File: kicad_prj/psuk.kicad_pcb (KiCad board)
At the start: 2 copper layers, 39 parts, among them J1 ATABA S-360-12 connector, J5 XT-60F, Q1 AOD240, Q2 AOD240, U1 OPA189IDR, U2 TL431DBZ, U3 TL431DBZ, U4 LM397

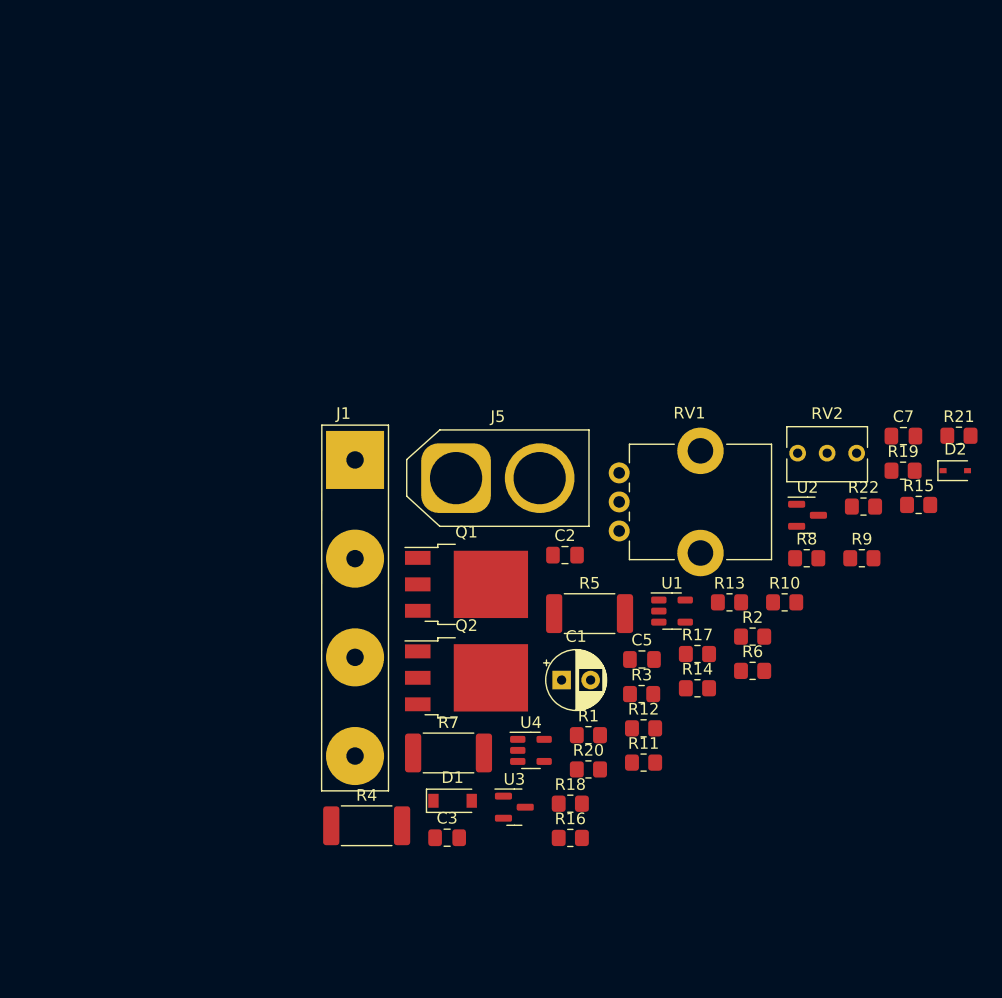
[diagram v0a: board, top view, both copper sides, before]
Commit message: Updated schematics. Fixed wrong and missing 3D models.
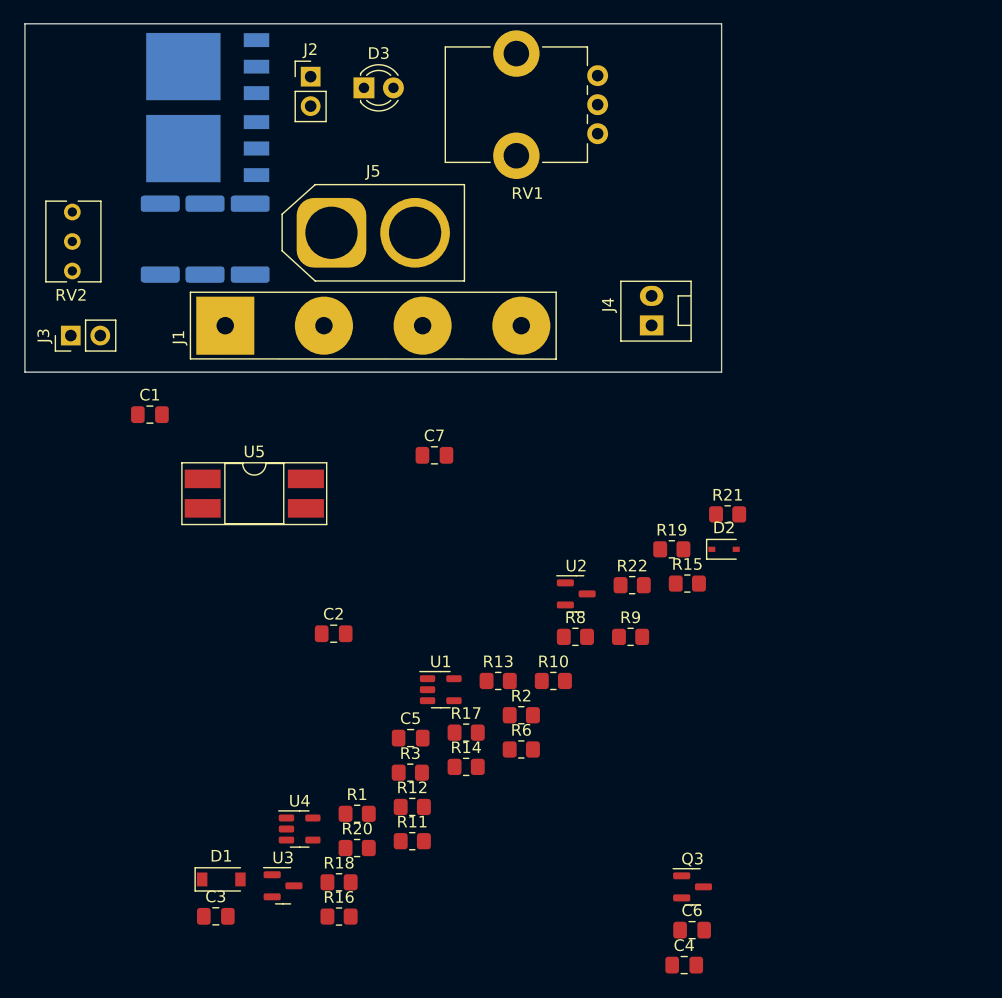
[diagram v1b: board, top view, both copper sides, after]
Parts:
- added C4: 150pF, Capacitor_SMD:C_0805_2012Metric_Pad1.18x1.45mm_HandSolder, F.Cu at (119.8, 121.1)
- added C6: 1n, Capacitor_SMD:C_0805_2012Metric_Pad1.18x1.45mm_HandSolder, F.Cu at (120.5, 118.1)
- added D3: YEL-3mm, LED_THT:LED_D3.0mm, F.Cu at (92.2, 45.5)
- added J2: 22-23-2021, Connector_PinHeader_2.54mm:PinHeader_1x02_P2.54mm_Vertical, F.Cu at (87.6, 44.6)
- added J3: 22-23-2021, Connector_PinHeader_2.54mm:PinHeader_1x02_P2.54mm_Vertical, F.Cu at (66.9, 66.9)
- added J4: XH2.54-2P, psuk:FanPinHeader_1x02_P2.54mm_Vertical, F.Cu at (117.0, 66.0)
- added Q3: IRLML2502TRPBF, Package_TO_SOT_SMD:SOT-23, F.Cu at (120.5, 114.3)
- added U5: FOD817B3SD, Package_DIP:DIP-4_W8.89mm_SMDSocket_LongPads, F.Cu at (82.8, 80.5)
- C1: value 22uF -> 10u/25V; footprint Capacitor_THT:CP_Radial_D5.0mm_P2.50mm -> Capacitor_SMD:C_0805_2012Metric_Pad1.18x1.45mm_HandSolder
- Q1, Q2, R4, R5, R7: moved to B.Cu
- moved RV2 70.7 mm to (67.1, 56.2), turned to 90 degrees
- moved R4 53.6 mm to (74.7, 58.5), turned to -90 degrees
- moved Q2 50.7 mm to (78.7, 50.7), turned to 180 degrees
- moved Q1 49.9 mm to (78.7, 43.7), turned to 180 degrees
- moved R7 47.4 mm to (82.4, 58.5), turned to -90 degrees
- moved R5 46.2 mm to (78.5, 58.5), turned to -90 degrees
- moved C1 42.2 mm to (73.8, 73.7)
- moved C7 40.4 mm to (98.3, 77.2)
- moved RV1 39.3 mm to (112.3, 44.5), turned to 180 degrees
- moved J5 23.7 mm to (89.4, 58.0)
- moved R8 21.0 mm to (110.4, 92.8)
- moved R9 21.0 mm to (115.2, 92.8)
- moved C3 21.0 mm to (79.4, 116.9)
- moved D2 21.0 mm to (123.2, 85.3)
- moved R1 21.0 mm to (91.6, 108.0)
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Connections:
- C1 pad 1: Net-(C1-Pad1) -> GND
- C1 pad 2: GND -> Net-(D1-Pad1)
- D1 pad 1: Net-(C1-Pad1) -> Net-(D1-Pad1)
- R1 pad 1: Net-(C1-Pad1) -> Net-(D1-Pad1)
- R2 pad 1: Net-(C1-Pad1) -> Net-(D1-Pad1)
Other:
- board outline added: 60 x 30 mm

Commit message: Completed PCB routing. Released v1.0 artifact for production and procurement purposes.
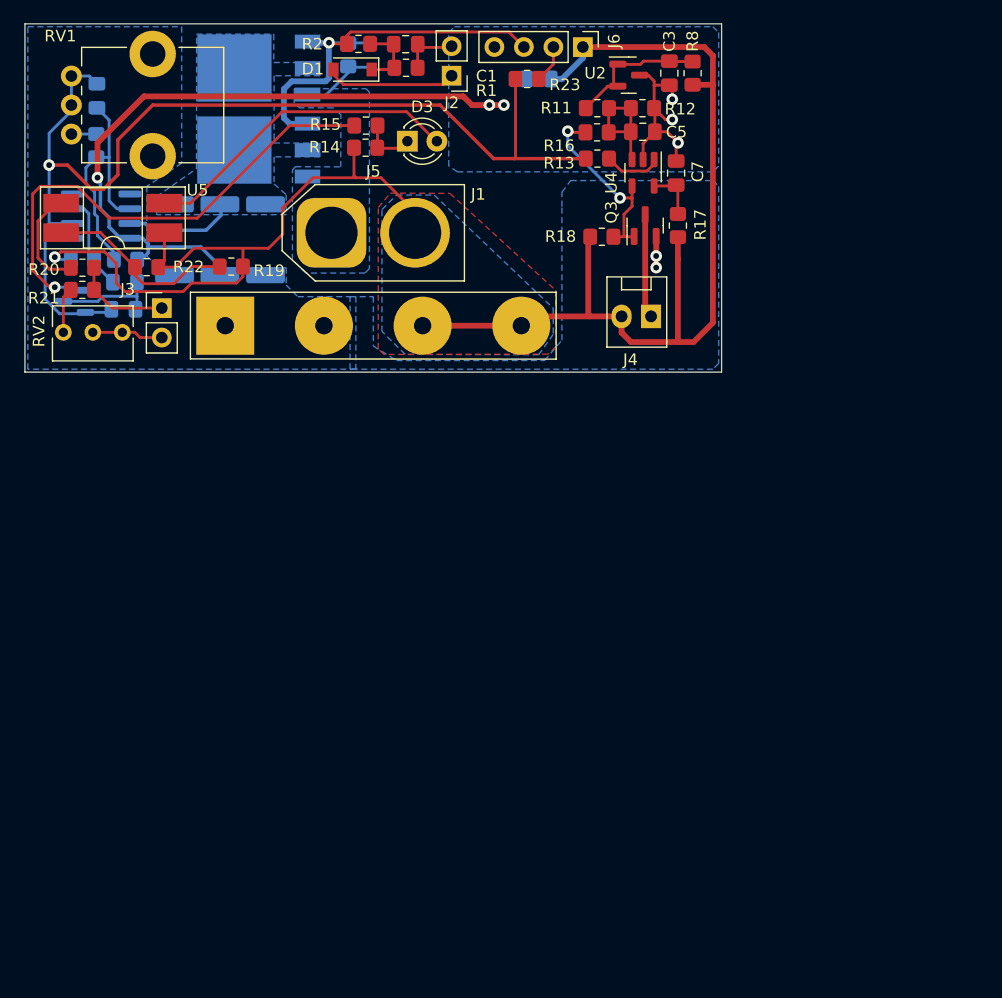
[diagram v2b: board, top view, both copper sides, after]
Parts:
- added C8: 100n, Capacitor_SMD:C_0805_2012Metric_Pad1.18x1.45mm_HandSolder, B.Cu at (107.2, 44.8)
- added J6: Conn_01x04_Male, Connector_PinHeader_2.54mm:PinHeader_1x04_P2.54mm_Vertical, F.Cu at (111.0, 42.0)
- added R23: 47, Resistor_SMD:R_0805_2012Metric_Pad1.20x1.40mm_HandSolder, F.Cu at (106.2, 44.8)
- C2, C4, C6, D2, R10, R3, R6, R9, U3: moved to B.Cu
- R16: value 220k -> 1M
- U1: footprint Package_TO_SOT_SMD:TSOT-23-5 -> Package_SO:SOIC-8_3.9x4.9mm_P1.27mm; moved to B.Cu
- moved C4 90.4 mm to (69.2, 46.2), turned to -90 degrees
- moved C3 82.5 mm to (118.5, 44.2), turned to 90 degrees
- moved C6 72.5 mm to (71.5, 64.6), turned to 180 degrees
- moved R16 71.1 mm to (112.3, 49.3), turned to 180 degrees
- moved D1 70.7 mm to (91.2, 43.9), turned to 180 degrees
- moved R11 65.1 mm to (112.3, 47.3)
- moved R1 64.4 mm to (95.8, 43.8)
- moved U4 63.8 mm to (116.2, 52.8), turned to -90 degrees
- moved R12 63.4 mm to (116.2, 47.3)
- moved R9 62.5 mm to (69.1, 50.5), turned to 90 degrees
- moved R3 62.1 mm to (90.8, 42.7), turned to -90 degrees
- moved R18 60.0 mm to (112.7, 58.3), turned to 180 degrees
- moved R2 59.5 mm to (91.7, 41.7), turned to 180 degrees
- moved R21 58.8 mm to (67.9, 62.9), turned to 180 degrees
- moved Q3 57.1 mm to (116.4, 57.4), turned to 90 degrees
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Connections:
- U1 pad 1: Net-(C4-Pad1) -> unconnected-(U1-Pad1)
- U1 pad 2: GND -> Net-(C4-Pad2)
- U1 pad 4: Net-(C4-Pad2) -> GND
- U1 pad 5: Net-(C2-Pad2) -> unconnected-(U1-Pad5)
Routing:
- net +12V: track 0.00 -> 142.7 mm, vias 0 -> 1
- net GND: track 0.00 -> 94.6 mm, vias 0 -> 8
- net Net-(C4-Pad1): track 0.00 -> 90.9 mm, vias 0 -> 1
- net Net-(R15-Pad2): track 0.00 -> 44.2 mm, vias 0 -> 1
- net Net-(D2-Pad1): track 0.00 -> 35.8 mm, vias 0 -> 1
- net Net-(D3-Pad2): track 0.00 -> 27.8 mm
- net Net-(C4-Pad2): track 0.00 -> 21.7 mm
- net Net-(Q3-Pad1): track 0.00 -> 16.7 mm, vias 0 -> 2
- net Net-(R19-Pad2): track 0.00 -> 16.5 mm
- net Net-(C3-Pad2): track 0.00 -> 12.0 mm
- net Net-(D1-Pad2): track 0.00 -> 11.3 mm
- net Net-(C5-Pad2): track 0.00 -> 10.4 mm
- net Net-(Q1-Pad2): track 0.00 -> 9.55 mm
- net Net-(R20-Pad1): track 0.00 -> 9.26 mm
- net Net-(J4-Pad1): track 0.00 -> 8.97 mm
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- added copper zone on B.Cu, net +12V
- added copper zone on F.Cu, net +12V
- added copper zone on B.Cu, net GND
- added copper zone on B.Cu, net Net-(D2-Pad2)
- added copper zone on B.Cu, net Net-(Q1-Pad2)
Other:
- board text added: "PSUK V1.0"
